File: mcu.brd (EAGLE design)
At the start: 37.2 x 57.6 mm, 67 parts, among them IC1 MCP73831/OT, T1 SI7051-A20, U12 BQ297XY, U4 NRF52832, U7 CP2102N-A01-GQFN24, X1 LFXTAL069526, X6 32.768kHz

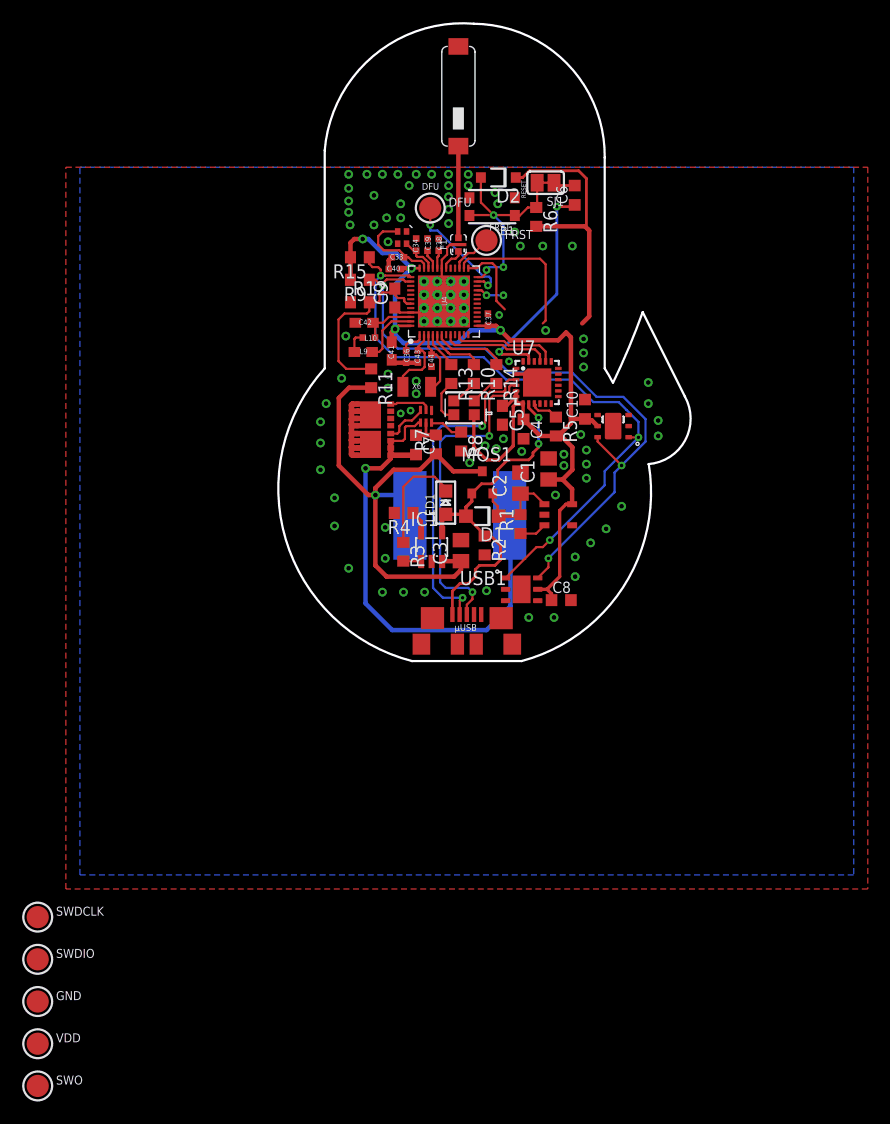
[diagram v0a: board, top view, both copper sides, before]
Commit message: UPD: usb position
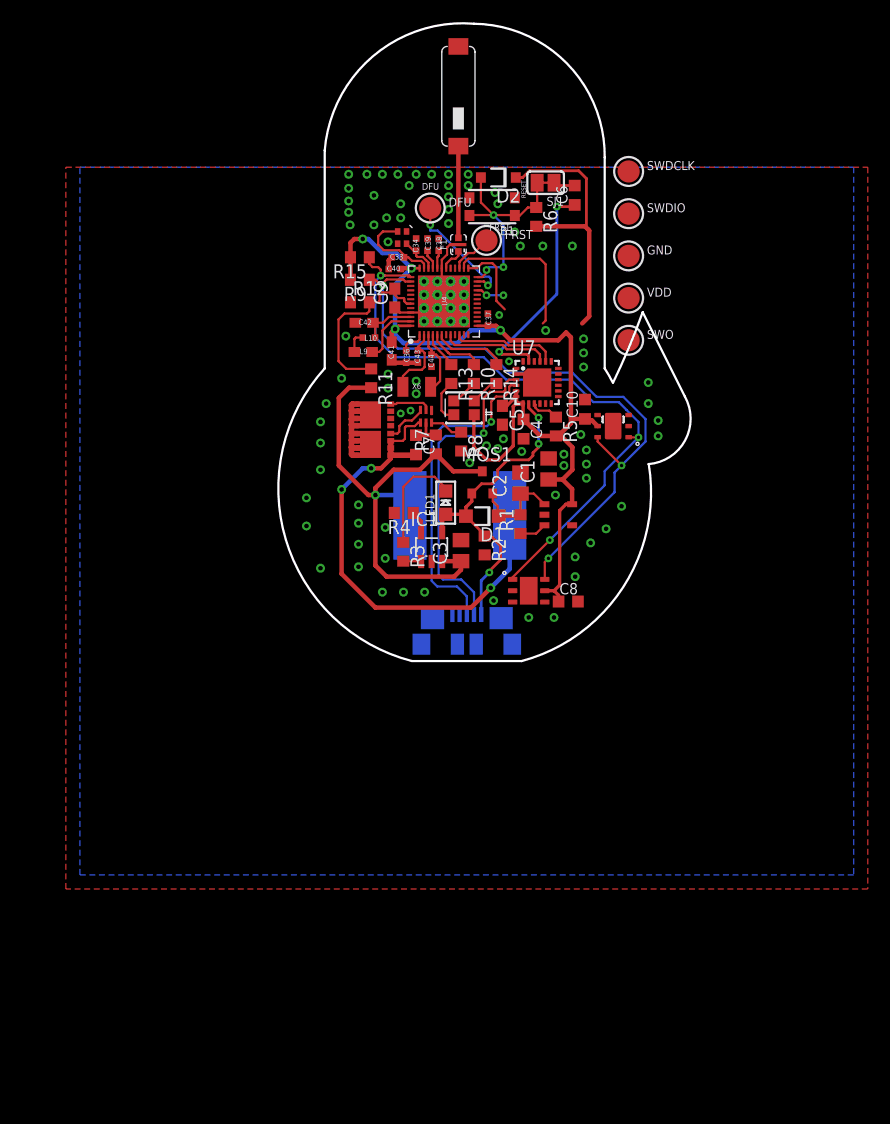
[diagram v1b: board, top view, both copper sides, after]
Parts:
- moved GND 85.9 mm to (67.3, 58.4)
- moved SWDCLK 85.9 mm to (67.3, 66.0)
- moved SWDIO 85.9 mm to (67.3, 62.2)
- moved SWO 85.9 mm to (67.3, 50.8)
- moved VDD 85.9 mm to (67.3, 54.6)
- moved T1 0.65 mm to (58.3, 28.2)
- moved C8 0.65 mm to (61.9, 27.2)
- flipped USB1 to the bottom
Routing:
- net VUSB: track 32.6 -> 30.3 mm, vias 2 -> 3
- net N$16: track 46.2 -> 44.2 mm, vias 1 -> 3
- net USBD+: track 29.9 -> 29.3 mm, vias 2 -> 1
- net USBD-: track 29.4 -> 29.3 mm, vias 2 -> 1
- net GND: vias 80 -> 84

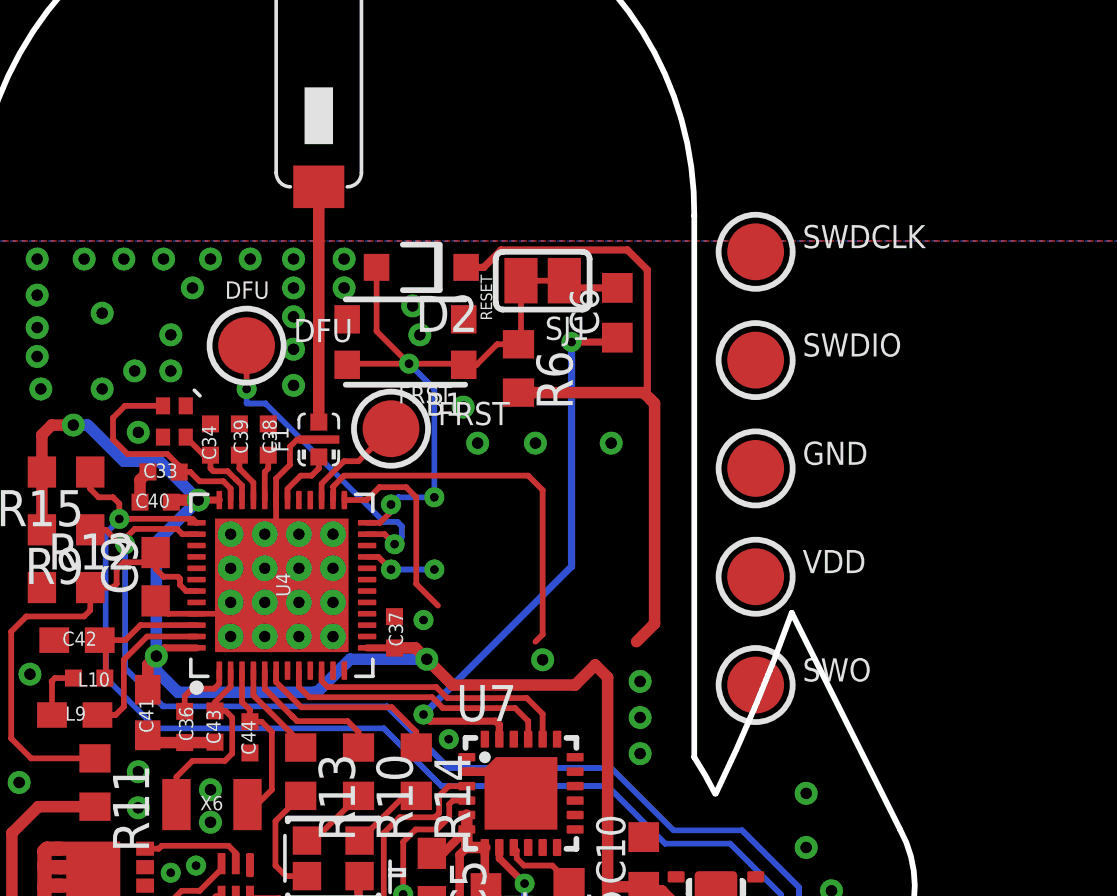
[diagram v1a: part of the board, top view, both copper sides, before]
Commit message: UPD: coplanar waveguide
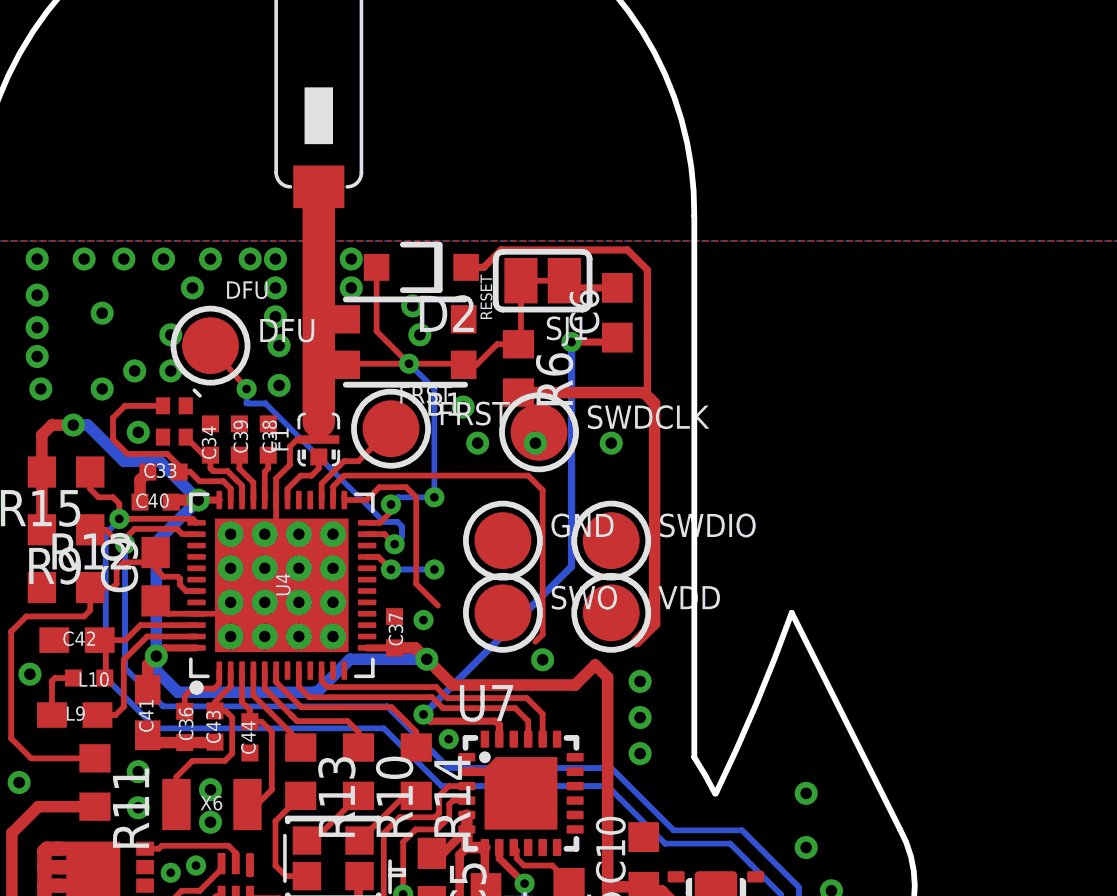
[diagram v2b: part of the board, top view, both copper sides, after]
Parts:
- moved SWDCLK 9.92 mm to (59.7, 59.7)
- moved SWO 9.25 mm to (58.4, 53.3)
- moved GND 9.25 mm to (58.4, 55.9)
- moved SWDIO 8.13 mm to (62.2, 55.9)
- moved VDD 5.24 mm to (62.2, 53.3)
- moved DFU 1.27 mm to (48.1, 62.7)
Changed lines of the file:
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@@
 <element name="B1" library="microbuilder" package="BTN_KMR2_4.6X2.8" value="" x="54.991" y="62.865" rot="R180"/>
 <element name="FRST" library="microbuilder" package="TESTPOINT_ROUND_2MM" value="" x="54.483" y="59.817"/>
-<element name="DFU" library="microbuilder" package="TESTPOINT_ROUND_2MM" value="" x="49.403" y="62.738"/>
+<element name="DFU" library="microbuilder" package="TESTPOINT_ROUND_2MM" value="" x="48.133" y="62.738"/>
 <element name="C7" library="rcl" library_urn="urn:adsk.eagle:library:334" package="C0603K" package3d_urn="urn:adsk.eagle:package:23680/2" value="0.1µF" x="48.119" y="41.362" rot="R270">
 <attribute name="SPICEPREFIX" value="C" x="48.119" y="41.362" size="1.778" layer="27" rot="R270" display="off"/>
@@
 <attribute name="SPICEPREFIX" value="C" x="63.373" y="44.577" size="1.778" layer="27" rot="R90" display="off"/>
 </element>
-<element name="SWDCLK" library="microbuilder" package="TESTPOINT_ROUND_2MM" value="" x="67.31" y="66.04"/>
-<element name="SWDIO" library="microbuilder" package="TESTPOINT_ROUND_2MM" value="" x="67.31" y="62.23"/>
-<element name="GND" library="microbuilder" package="TESTPOINT_ROUND_2MM" value="" x="67.31" y="58.42"/>
-<element name="VDD" library="microbuilder" package="TESTPOINT_ROUND_2MM" value="" x="67.31" y="54.61"/>
-<element name="SWO" library="microbuilder" package="TESTPOINT_ROUND_2MM" value="" x="67.31" y="50.8"/>
+<element name="SWDCLK" library="microbuilder" package="TESTPOINT_ROUND_2MM" value="" x="59.69" y="59.69"/>
+<element name="SWDIO" library="microbuilder" package="TESTPOINT_ROUND_2MM" value="" x="62.23" y="55.88"/>
+<element name="GND" library="microbuilder" package="TESTPOINT_ROUND_2MM" value="" x="58.42" y="55.88"/>
+<element name="VDD" library="microbuilder" package="TESTPOINT_ROUND_2MM" value="" x="62.23" y="53.34"/>
+<element name="SWO" library="microbuilder" package="TESTPOINT_ROUND_2MM" value="" x="58.42" y="53.34"/>
 </elements>
 <signals>
@@
 <via x="61.468" y="40.513" extent="1-16" drill="0.4064"/>
 <via x="61.468" y="39.497" extent="1-16" drill="0.4064"/>
-<via x="52.832" y="65.786" extent="1-16" drill="0.4064"/>
-<via x="51.054" y="65.786" extent="1-16" drill="0.4064"/>
+<via x="53.086" y="65.786" extent="1-16" drill="0.4064"/>
+<via x="50.419" y="65.786" extent="1-16" drill="0.4064"/>
 <via x="63.5" y="39.624" extent="1-16" drill="0.4064"/>
 <via x="63.5" y="40.894" extent="1-16" drill="0.4064"/>
@@
 <via x="69.977" y="43.561" extent="1-16" drill="0.4064"/>
 <via x="69.977" y="42.164" extent="1-16" drill="0.4064"/>
-<via x="51.054" y="63.754" extent="1-16" drill="0.4064"/>
-<via x="51.054" y="61.341" extent="1-16" drill="0.4064"/>
-<via x="52.832" y="64.77" extent="1-16" drill="0.4064"/>
-<via x="51.054" y="62.611" extent="1-16" drill="0.4064"/>
-<via x="51.054" y="64.77" extent="1-16" drill="0.4064"/>
+<via x="50.419" y="63.754" extent="1-16" drill="0.4064"/>
+<via x="50.546" y="61.341" extent="1-16" drill="0.4064"/>
+<via x="53.086" y="64.77" extent="1-16" drill="0.4064"/>
+<via x="50.546" y="62.738" extent="1-16" drill="0.4064"/>
+<via x="50.419" y="64.77" extent="1-16" drill="0.4064"/>
 <via x="45.466" y="61.849" extent="1-16" drill="0.4064"/>
 <via x="46.736" y="61.849" extent="1-16" drill="0.4064"/>
@@
 <via x="42.926" y="32.385" extent="1-16" drill="0.4064"/>
 <via x="42.926" y="30.353" extent="1-16" drill="0.4064"/>
-<wire x1="62.23" y1="59.309" x2="67.31" y2="58.42" width="0" layer="19" extent="1-1"/>
 </signal>
 <signal name="SWDIO">
@@
 <wire x1="59.817" y1="52.578" x2="59.563" y2="52.324" width="0.2032" layer="1"/>
 <contactref element="SWDIO" pad="P$1"/>
-<wire x1="59.817" y1="57.658" x2="67.31" y2="62.23" width="0" layer="19" extent="1-1"/>
+<wire x1="59.817" y1="57.658" x2="62.23" y2="55.88" width="0" layer="19" extent="1-1"/>
 </signal>
 <signal name="DEC1">
@@
 <wire x1="55.0164" y1="57.7596" x2="55.372" y2="57.404" width="0.2032" layer="1"/>
 <contactref element="SWDCLK" pad="P$1"/>
-<wire x1="55.372" y1="57.404" x2="67.31" y2="66.04" width="0" layer="19" extent="1-1"/>
+<wire x1="55.372" y1="57.404" x2="59.69" y2="59.69" width="0" layer="19" extent="1-1"/>
 </signal>
 <signal name="N$8">
@@
 <wire x1="54.483" y1="54.864" x2="56.007" y2="54.864" width="0.2032" layer="16"/>
 <contactref element="SWO" pad="P$1"/>
-<wire x1="56.007" y1="54.864" x2="67.31" y2="50.8" width="0" layer="19" extent="1-1"/>
+<wire x1="56.007" y1="54.864" x2="58.42" y2="53.34" width="0" layer="19" extent="1-1"/>
 </signal>
 <signal name="P0.19">
@@
 <via x="49.403" y="61.214" extent="1-16" drill="0.3048"/>
 <wire x1="50.06489375" y1="60.706" x2="49.403" y2="60.706" width="0.2032" layer="16"/>
-<wire x1="49.403" y1="61.214" x2="49.403" y2="62.738" width="0.2032" layer="1"/>
+<wire x1="49.403" y1="61.214" x2="48.133" y2="62.738" width="0.2032" layer="1"/>
 </signal>
 <signal name="P0.21/RESET">
@@
 <contactref element="ANT1" pad="1"/>
 <contactref element="F1" pad="3"/>
-<wire x1="51.943" y1="60.0485" x2="51.943" y2="68.326" width="0.4064" layer="1"/>
+<wire x1="51.943" y1="60.0485" x2="51.943" y2="68.326" width="1.143" layer="1"/>
 </signal>
 <signal name="P0.09">
@@
 <wire x1="61.087" y1="28.702" x2="60.579" y2="28.194" width="0.3048" layer="1"/>
 <wire x1="61.087" y1="35.433" x2="61.087" y2="28.702" width="0.3048" layer="1"/>
-<wire x1="63.754" y1="52.959" x2="67.31" y2="54.61" width="0" layer="19" extent="1-1"/>
+<wire x1="63.119" y1="52.324" x2="62.23" y2="53.34" width="0" layer="19" extent="1-1"/>
 <wire x1="62.103" y1="51.071" x2="63.119" y2="52.324" width="0" layer="19" extent="1-1"/>
 </signal>

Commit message: UPD: board, and RF line
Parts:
- removed VDD: (no value), microbuilder:TESTPOINT_ROUND_2MM
- added R16: 0, rcl:R0402
- added R17, R18: DNP, rcl:R0402
- moved GND 16.9 mm to (43.8, 64.4)
- moved D2 12.4 mm to (58.2, 53.4), turned to 90 degrees
- moved B1 10.8 mm to (61.0, 53.8), turned to 270 degrees
- moved SWDIO 9.28 mm to (57.5, 63.9)
- moved R6 8.59 mm to (56.2, 53.8)
- moved SJ1 7.31 mm to (60.8, 57.8)
- moved C6 4.51 mm to (60.7, 59.7), turned to 0 degrees
- moved SWO 3.98 mm to (56.6, 56.9)
- moved SWDCLK 2.77 mm to (60.5, 62.4)
- moved DFU 2.19 mm to (46.0, 62.4)
- moved FRST 1.70 mm to (55.2, 61.3)
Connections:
- new net N$18: ANT1.1, R16.2, R17.2
- net GND: now also R17.1, R18.1
- net RF: now also R16.1, R18.2; no longer ANT1.1
- net V+: no longer VDD.P$1
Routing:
- net V+: track 118.1 -> 94.1 mm
- net RF: track 8.28 -> 0.00 mm
- net DTR: track 20.3 -> 16.0 mm
- net SWDIO: track 13.7 -> 9.80 mm
- net SWDCLK: track 7.19 -> 10.1 mm
- net P0.22: track 3.82 -> 5.81 mm
- net P0.20: track 11.6 -> 13.2 mm
- net P0.18/SWO: track 2.55 -> 3.79 mm, vias 2 -> 0
- net P0.21/RESET: track 20.4 -> 19.4 mm, vias 3 -> 0
- net GND: vias 84 -> 87
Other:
- board text added: "SWO"
- board text added: "VDD"

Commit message: UPD: feed
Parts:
- moved R18 0.89 mm to (51.3, 62.5)
- moved R16 0.38 mm to (51.9, 64.1)
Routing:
- net GND: track 31.9 -> 29.1 mm
- net RF: track 0.00 -> 0.53 mm
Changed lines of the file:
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@@
 <element name="GND" library="microbuilder" package="TESTPOINT_ROUND_2MM" value="" x="43.815" y="64.389"/>
 <element name="SWO" library="microbuilder" package="TESTPOINT_ROUND_2MM" value="" x="56.642" y="56.896"/>
-<element name="R16" library="rcl" library_urn="urn:adsk.eagle:library:334" package="R0402" package3d_urn="urn:adsk.eagle:package:23547/2" value="0" x="51.943" y="63.754" rot="R90">
-<attribute name="SPICEPREFIX" value="R" x="51.943" y="63.754" size="0.6096" layer="27" rot="R90" display="off"/>
+<element name="R16" library="rcl" library_urn="urn:adsk.eagle:library:334" package="R0402" package3d_urn="urn:adsk.eagle:package:23547/2" value="0" x="51.943" y="64.135" rot="R90">
+<attribute name="SPICEPREFIX" value="R" x="51.943" y="64.135" size="0.6096" layer="27" rot="R90" display="off"/>
 </element>
 <element name="R17" library="rcl" library_urn="urn:adsk.eagle:library:334" package="R0402" package3d_urn="urn:adsk.eagle:package:23547/2" value="DNP" x="51.308" y="65.786">
 <attribute name="SPICEPREFIX" value="R" x="51.308" y="65.786" size="0.6096" layer="27" display="off"/>
 </element>
-<element name="R18" library="rcl" library_urn="urn:adsk.eagle:library:334" package="R0402" package3d_urn="urn:adsk.eagle:package:23547/2" value="DNP" x="51.308" y="61.595">
-<attribute name="SPICEPREFIX" value="R" x="51.308" y="61.595" size="0.6096" layer="27" display="off"/>
+<element name="R18" library="rcl" library_urn="urn:adsk.eagle:library:334" package="R0402" package3d_urn="urn:adsk.eagle:package:23547/2" value="DNP" x="51.308" y="62.484">
+<attribute name="SPICEPREFIX" value="R" x="51.308" y="62.484" size="0.6096" layer="27" display="off"/>
 </element>
 </elements>
@@
 <wire x1="45.932" y1="58.293" x2="45.654" y2="58.015" width="0.4064" layer="1"/>
 <wire x1="45.654" y1="58.015" x2="45.654" y2="57.234" width="0.4064" layer="1"/>
-<wire x1="50.442" y1="57.307" x2="50.442" y2="58.062" width="0.2032" layer="1"/>
-<wire x1="50.442" y1="58.062" x2="50.927" y2="58.547" width="0.2032" layer="1"/>
-<wire x1="50.927" y1="58.547" x2="50.927" y2="59.182" width="0.2032" layer="1"/>
-<wire x1="50.927" y1="59.182" x2="51.181" y2="59.436" width="0.2032" layer="1"/>
-<wire x1="51.181" y1="59.436" x2="51.5805" y2="59.436" width="0.2032" layer="1"/>
 <via x="41.783" y="51.181" extent="1-16" drill="0.4064"/>
 <via x="55.499" y="41.021" extent="1-16" drill="0.4064"/>
@@
 <contactref element="R16" pad="1"/>
 <contactref element="R18" pad="2"/>
-<wire x1="51.808" y1="61.595" x2="51.943" y2="63.254" width="0" layer="19" extent="1-1"/>
-<wire x1="51.943" y1="60.0485" x2="51.808" y2="61.595" width="0" layer="19" extent="1-1"/>
+<wire x1="51.943" y1="60.0485" x2="51.943" y2="60.579" width="0.6096" layer="1"/>
+<wire x1="51.943" y1="63.635" x2="51.808" y2="62.484" width="0" layer="19" extent="1-1"/>
+<wire x1="51.943" y1="60.579" x2="51.808" y2="62.484" width="0" layer="19" extent="1-1"/>
 </signal>
 <signal name="P0.09">
@@
 <wire x1="50.842" y1="57.307" x2="50.842" y2="57.7" width="0.2032" layer="1"/>
 <wire x1="51.308" y1="58.166" x2="51.689" y2="58.166" width="0.254" layer="1"/>
-<wire x1="51.689" y1="58.166" x2="51.943" y2="58.42" width="0.254" layer="1"/>
+<wire x1="51.689" y1="58.166" x2="51.943" y2="58.42" width="0.3048" layer="1"/>
 <wire x1="51.943" y1="58.42" x2="51.943" y2="58.8235" width="0.3048" layer="1"/>
 <wire x1="50.842" y1="57.7" x2="51.308" y2="58.166" width="0.2032" layer="1"/>
@@
 <contactref element="R16" pad="2"/>
 <contactref element="R17" pad="2"/>
-<wire x1="51.808" y1="65.786" x2="51.943" y2="68.326" width="0" layer="19" extent="1-1"/>
-<wire x1="51.943" y1="64.254" x2="51.808" y2="65.786" width="0" layer="19" extent="1-1"/>
+<wire x1="51.943" y1="68.326" x2="51.943" y2="64.635" width="0" layer="19" extent="1-16"/>
+<wire x1="51.943" y1="64.635" x2="51.808" y2="65.786" width="0" layer="19" extent="1-1"/>
 </signal>
 </signals>

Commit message: UPD: battery
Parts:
- removed H1: HDC1080, tilesPartComp:PWSON_DMB
- added HU1: HDC2010, tilesPartComp:DSBGA-6
- R4: value 10K -> 37K
- U$14: value GM351824 -> GM171538; device tilesPartComp:GM351824 -> tilesPartComp:GM171538
- moved U$14 10.4 mm to (52.7, 28.7)
- moved R18 0.20 mm to (51.3, 62.7)
- moved R16 0.10 mm to (51.9, 64.2)
- flipped USB1 to the top
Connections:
- net N$16 renamed CBAT
- net GND: now also HU1.C1; no longer H1.2
- net P0.25: now also HU1.A2; no longer H1.1
- net P0.26: now also HU1.B2; no longer H1.6
- net V+: now also HU1.A1, HU1.B1; no longer H1.5
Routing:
- net CBAT: track 44.2 -> 29.8 mm
- net USBD+: track 29.3 -> 35.1 mm, vias 1 -> 2
- net N$18: track 0.00 -> 4.28 mm
- net VBAT: track 47.9 -> 52.0 mm
- net RF: track 0.53 -> 4.18 mm
- net USBD-: track 29.3 -> 32.3 mm, vias 1 -> 2
- net GND: track 29.1 -> 31.7 mm, vias 87 -> 104
- net N$4: track 9.91 -> 12.4 mm
- net VUSB: track 30.3 -> 32.2 mm, vias 3 -> 2
- net V+: track 94.1 -> 95.4 mm
- net P0.25: track 57.7 -> 58.5 mm
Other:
- board size 37.2 x 57.6 mm -> 36.7 x 57.5 mm

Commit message: UPD: finished before moving left area
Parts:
- removed C7: 0.1µF, rcl:C0603K
- removed CHG, DSG: CSD16406Q3, tilesPartComp:VSON-CLIP-8
- removed R7: 330, rcl:R0603
- removed R8: 2.2K, rcl:R0603
- removed U$14: GM171538, tilesPartComp:GM171538
- removed U12: BQ297XY, tilesPartComp:WSON_6
- added TEST1, TEST2: TESTPOINT_SQUARE_SMT, tilesPartComp:TESTPOINT_SMT
- moved R4 1.65 mm to (48.6, 35.8), turned to 90 degrees
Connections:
- removed net CBAT: C7.2, DSG.1, DSG.2, DSG.3, U$14.-, U12.4
- removed net N$11: CHG.5, CHG.6, CHG.7, CHG.8, CHG.EXP, DSG.5, DSG.6, DSG.7, DSG.8, DSG.EXP
- removed net N$12: DSG.4, U12.3
- removed net N$13: C7.1, R7.2, U12.5
- removed net N$14: CHG.4, U12.2
- removed net N$15: R8.1, U12.6
- net GND: now also TEST2.T; no longer CHG.1, CHG.2, CHG.3, R8.2
- net VBAT: now also TEST1.T; no longer R7.1, U$14.+
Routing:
- net CBAT: track 29.8 -> 0.00 mm, vias 3 -> 0
- net N$11: track 11.7 -> 0.00 mm
- net VBAT: track 52.0 -> 43.9 mm
- net N$12: track 3.98 -> 0.00 mm
- net N$4: track 12.4 -> 8.49 mm
- net N$14: track 3.71 -> 0.00 mm
- net P0.25: track 58.5 -> 61.9 mm
- net N$15: track 3.03 -> 0.00 mm
- net N$13: track 2.93 -> 0.00 mm
- net P0.26: track 56.9 -> 59.8 mm
- net N$6: track 2.15 -> 1.59 mm
- net GND: vias 104 -> 101
- added copper zone on layer 1, net N$11
- added copper zone on layer 16, net N$12
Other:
- board text added: "BAT+"
- board text added: "BAT-"
- board text added: "GND"
- board text added: "SWDCLK"
- board text added: "SWDIO"
- board text added: "TilesTemp v1.0 ISSE-IDI-NTNU Trondheim Francesco Gianni, Monica Divitini Welle Design"
